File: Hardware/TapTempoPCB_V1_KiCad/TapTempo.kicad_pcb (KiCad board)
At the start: 2 copper layers, 50 x 50 mm, 15 parts, among them P1 CONN_2, P2 CONN_5, P3 CONN_6, P4 CONN_1, P5 CONN_1, Q1 2N3904, U2 PIC12F1822

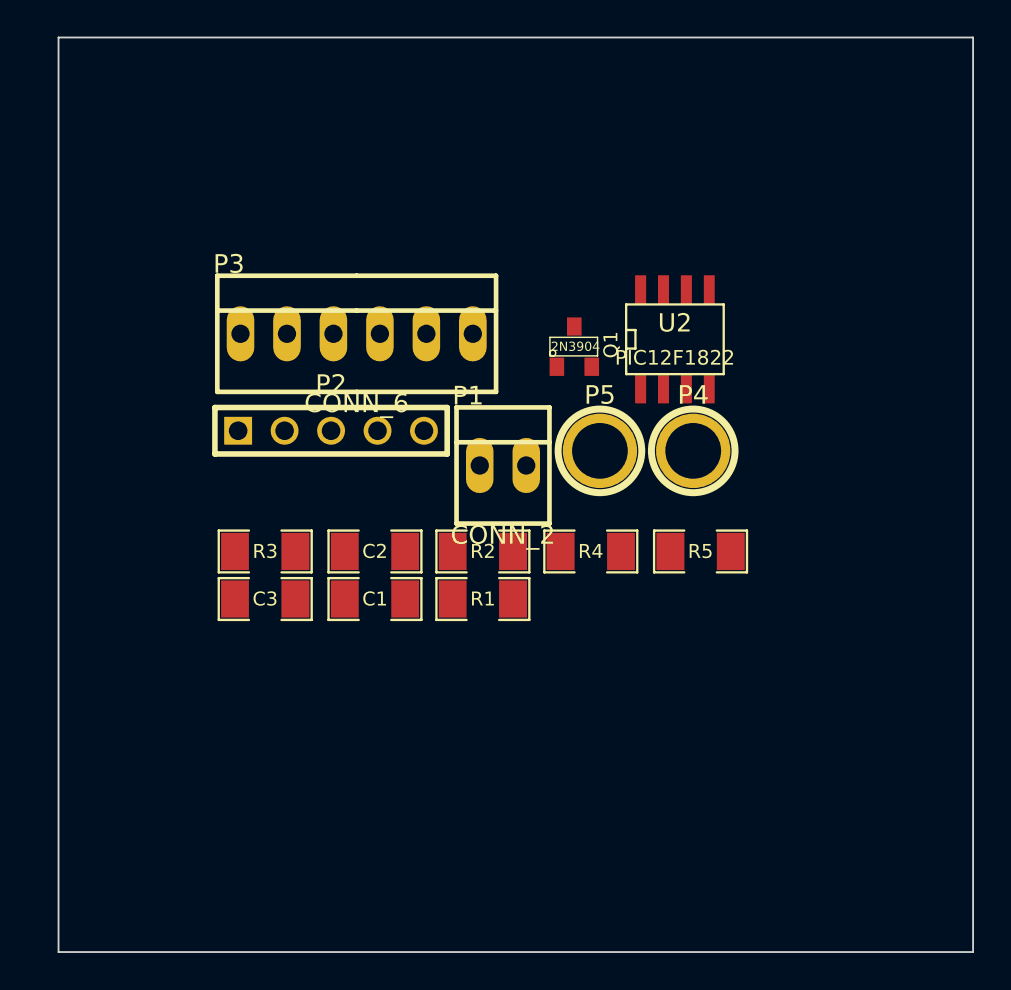
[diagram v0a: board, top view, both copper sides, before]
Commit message: Added LUT table to firmware for VCO also added spreadsheet for LUT
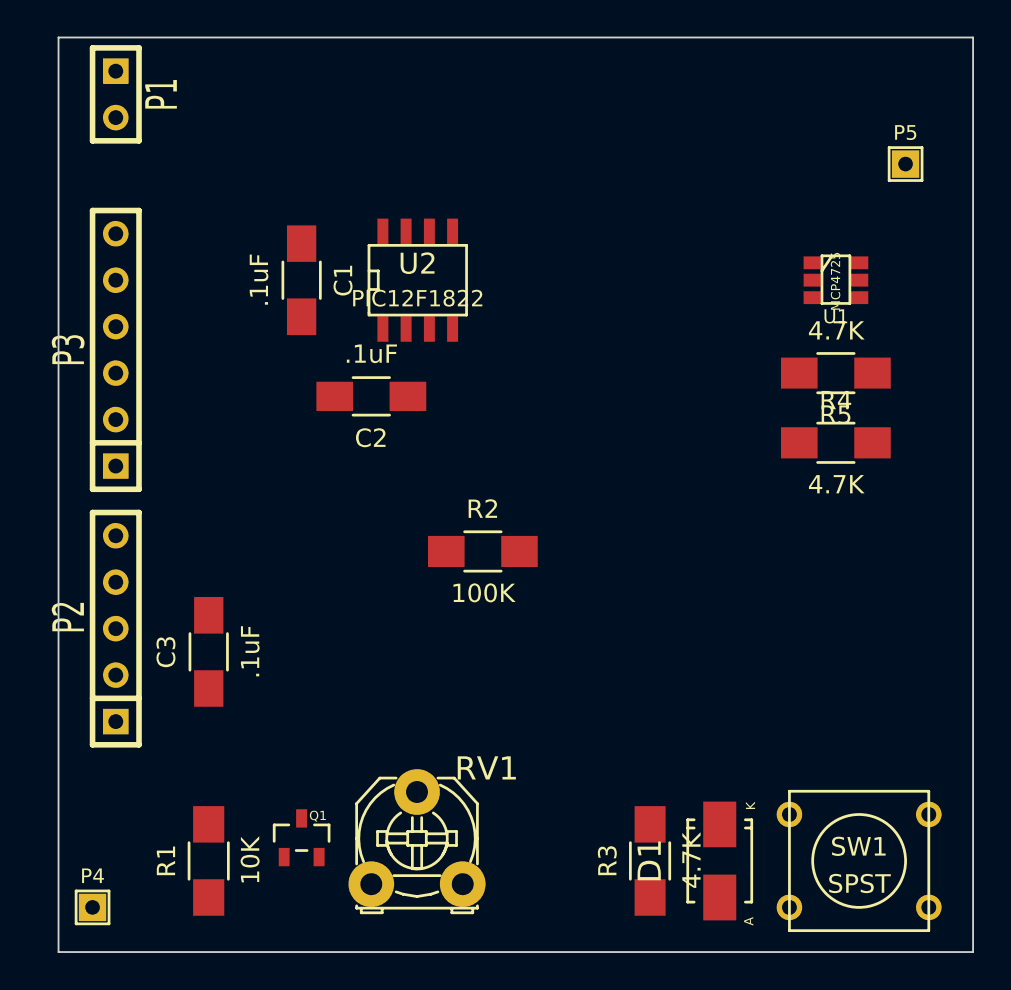
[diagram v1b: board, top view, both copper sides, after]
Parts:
- added D1: DIODE, Diodes_SMD:Diode-SMA_Standard, F.Cu at (222.2, 160.0)
- added RV1: POT, Potentiometers:Potentiometer_Triwood_RM-065, F.Cu at (203.2, 161.3)
- added SW1: SPST, Discret:SW_PUSH_SMALL, F.Cu at (229.9, 160.0)
- added U1: MCP4725, SMD_Packages:SOT-23-6, F.Cu at (228.6, 128.3)
- C1, C3: value C -> .1uF; footprint SM1206 -> Capacitors_SMD:C_1206_HandSoldering
- C2: footprint SM1206 -> Capacitors_SMD:C_1206_HandSoldering
- P1: footprint PINHEAD1-2 -> Connect:SIL-2
- P2: footprint PIN_ARRAY_5x1 -> Connect:SIL-5
- P3: footprint PINHEAD1-6 -> Connect:SIL-6
- P4, P5: footprint 1pin -> Connect:SIL-1
- Q1: footprint SOT23 -> Transistors_SMD:sot23
- R1, R2, R3, R4, R5: footprint SM1206 -> Resistors_SMD:R_1206_HandSoldering
- U2: footprint SOIC-8_N -> SMD_Packages:SOIC-8-W
- moved P4 41.2 mm to (188.0, 162.6)
- moved Q1 30.7 mm to (199.4, 158.8)
- moved P1 29.3 mm to (189.2, 118.1), turned to 270 degrees
- moved R3 27.0 mm to (218.4, 160.0), turned to 90 degrees
- moved P5 22.9 mm to (232.4, 121.9)
- moved R1 20.7 mm to (194.3, 160.0), turned to 90 degrees
- moved C1 17.9 mm to (199.4, 128.3), turned to 270 degrees
- moved P2 15.2 mm to (189.2, 146.1), turned to 90 degrees
- moved R4 14.7 mm to (228.6, 137.2)
- moved U2 14.4 mm to (205.7, 128.3)
- moved P3 13.2 mm to (189.2, 132.1), turned to 90 degrees
- moved R5 12.2 mm to (228.6, 133.3), turned to 180 degrees
- moved C2 8.48 mm to (203.2, 134.6), turned to 180 degrees
- moved C3 4.23 mm to (194.3, 148.6), turned to 90 degrees
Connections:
- net PGC renamed SCL
- Q1 pad 1: (no net) -> Net-(Q1-Pad1)
- R1 pad 2: (no net) -> Net-(Q1-Pad1)

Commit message: Lots of changes to the TapTempo Board, made it all consistantly surface mount, turned into a module and created gerbers.
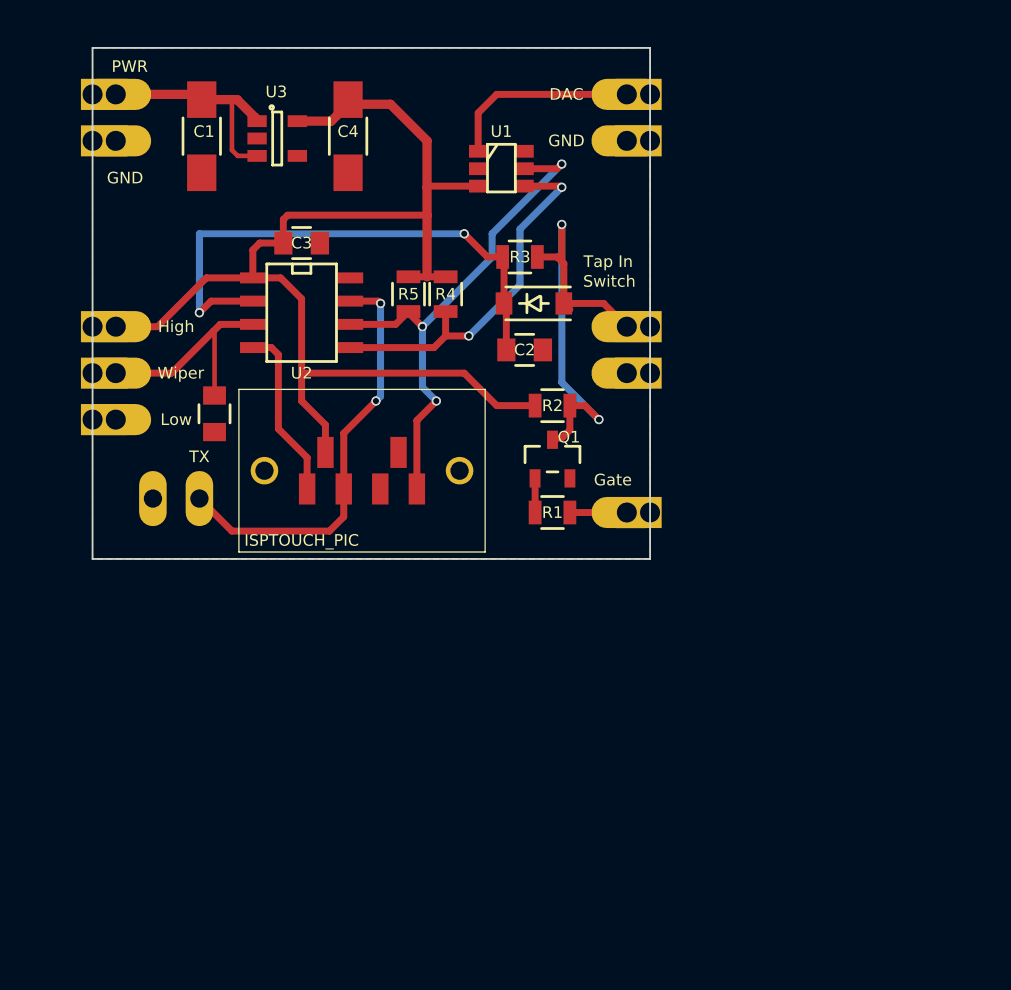
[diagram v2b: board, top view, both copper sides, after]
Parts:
- removed RV1: POT, Potentiometers:Potentiometer_Triwood_RM-065
- removed SW1: SPST, Discret:SW_PUSH_SMALL
- added ?: , SoulySolarLogo, B.Cu at (207.5, 131.3)
- added C4: 1uF, Capacitors_SMD:C_1206_HandSoldering, F.Cu at (201.9, 120.4)
- added C5: .1uF, Capacitors_SMD:C_0805, F.Cu at (194.6, 135.6)
- added J1: ISPTOUCH_PIC, ICSP_TOUCH_AVX_9188_6-WAY_MATING_GUIDE, F.Cu at (202.7, 138.7)
- added P10: Low, My_Library:Castellation, F.Cu at (188.0, 135.9)
- added P11: GND, My_Library:Castellation, F.Cu at (218.4, 120.7)
- added P6: Switch_1, My_Library:Castellation, F.Cu at (218.4, 130.8)
- added P7: Switch_2, My_Library:Castellation, F.Cu at (218.4, 133.3)
- added P8: High, My_Library:Castellation, F.Cu at (188.0, 130.8)
- added P9: Wiper, My_Library:Castellation, F.Cu at (188.0, 133.3)
- added U3: LDK220, Housings_SOT-23_SOT-143_TSOT-6:SOT-23-5, F.Cu at (198.1, 120.5)
- C1: value .1uF -> 1uF
- C2, C3: footprint Capacitors_SMD:C_1206_HandSoldering -> Capacitors_SMD:C_0805
- D1: footprint Diodes_SMD:Diode-SMA_Standard -> Diodes_SMD:SOD-123
- P1: value CONN_2 -> PWR; footprint Connect:SIL-2 -> My_Library:Castellation
- P2: value CONN_5 -> GND; footprint Connect:SIL-5 -> My_Library:Castellation
- P3: value CONN_6 -> CONN_01X02; footprint Connect:SIL-6 -> Connect:PINHEAD1-2
- P4: value CONN_1 -> DAC; footprint Connect:SIL-1 -> My_Library:Castellation
- P5: value CONN_1 -> Gate; footprint Connect:SIL-1 -> My_Library:Castellation
- R1, R2, R3, R4, R5: footprint Resistors_SMD:R_1206_HandSoldering -> My_Library:R_0805
- moved P4 53.9 mm to (218.4, 118.1), turned to 90 degrees
- moved R3 33.8 mm to (211.3, 127.0), turned to 180 degrees
- moved D1 32.1 mm to (212.1, 129.5), turned to 180 degrees
- moved R1 26.8 mm to (213.1, 141.0), turned to 180 degrees
- moved P2 25.4 mm to (188.0, 120.7), turned to 270 degrees
- moved Q1 24.8 mm to (213.1, 138.0)
- moved R5 23.8 mm to (205.2, 129.0), turned to 90 degrees
- moved P5 23.6 mm to (218.4, 141.0), turned to 90 degrees
- moved C3 22.9 mm to (199.4, 126.2), turned to 0 degrees
- moved R4 22.8 mm to (207.3, 129.0), turned to 270 degrees
- moved U1 19.3 mm to (210.3, 122.2)
- moved C1 9.58 mm to (193.9, 120.4), turned to 90 degrees
- moved R2 8.83 mm to (213.1, 135.1)
- moved P3 8.77 mm to (192.5, 140.2), turned to 0 degrees
- moved C2 8.76 mm to (211.6, 132.1), turned to 0 degrees
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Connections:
- C1 pad 2: VCC -> Net-(C1-Pad2)
- P1 pad 1: VCC -> Net-(C1-Pad2)
- P2 pad 1: MCLR -> GND
- P3 pad 2: (no net) -> PGD
- P4 pad 1: Gatein -> Net-(P4-Pad1)
- P5 pad 1: Net-(P5-Pad1) -> Gatein
- R5 pad 1: SCL -> PGC
- U1 pad 1: Net-(P5-Pad1) -> Net-(P4-Pad1)
- U1 pad 5: SCL -> PGC
- U2 pad 6: SCL -> PGC
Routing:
- net VCC: track 0.00 -> 67.4 mm
- net TAP: track 0.00 -> 29.8 mm, vias 0 -> 2
- net PGC: track 0.00 -> 28.4 mm, vias 0 -> 3
- net Net-(D1-Pad1): track 0.00 -> 26.3 mm, vias 0 -> 2
- net PGD: track 0.00 -> 23.2 mm, vias 0 -> 2
- net SDA: track 0.00 -> 20.4 mm, vias 0 -> 2
- net Net-(C1-Pad2): track 0.00 -> 12.6 mm
- net POT: track 0.00 -> 12.5 mm
- net Net-(P4-Pad1): track 0.00 -> 10.6 mm
- net MCLR: track 0.00 -> 9.55 mm
- net Gatein: track 0.00 -> 3.14 mm
- net Net-(Q1-Pad1): track 0.00 -> 1.87 mm
- added copper zone on F.Cu, net GND
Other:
- board size 50 x 50 mm -> 30.5 x 27.9 mm
- net class Default: clearance 0.254 -> 0.1524
- rule trace_clearance: 0.254 -> 0.1524
- rule trace_min: 0.254 -> 0.2032
- rule via_min_drill: 0.508 -> 0.254
- rule via_min_size: 0.889 -> 0.508
- board text added: "EAR TapTempo V1 6-2015"
- board text added: "Switch"
- board text added: "TX"
- board text added: "Tap In"
